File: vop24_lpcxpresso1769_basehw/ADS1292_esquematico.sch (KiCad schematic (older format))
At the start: 50 parts, among them J401 Conn_01x02, J402 Conn_01x02, J403 Conn_01x02, J404 Conn_01x04, J405 Conn_01x04, J406 Conn_01x04, U401 ADS1292, U402 LM334, U403 LM334, U404 LM334

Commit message: Finalizada asociación de todos los footprints. Ver librerías froux-kicad
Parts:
- C401, C402, C403, C404, C405, C406, C407, C408, C409, C410, C411, C412, C413, C414, C415, C416, C417, C418, C419, C420: footprint (none) -> Capacitor_SMD:C_0805_2012Metric_Pad1.15x1.40mm_HandSolder
- J401, J402, J403: footprint (none) -> Connector_PinHeader_1.27mm:PinHeader_1x02_P1.27mm_Vertical
- J404, J405, J406: footprint (none) -> Connector_PinHeader_1.27mm:PinHeader_1x04_P1.27mm_Vertical
- R401, R402, R403, R404, R405, R406, R407, R408, R409, R410, R411, R412, R413, R414, R415, R416, R417, R418, R419, R420: footprint (none) -> Resistor_SMD:R_0805_2012Metric_Pad1.15x1.40mm_HandSolder

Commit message: PCB: componentes agrupados por zona
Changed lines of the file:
@@
 SENS1N
 Text Label 10400 1650 0    60   ~ 0
-SENS1N
+SENS1P
 Wire Wire Line
 	6200 3250 6700 3250
@@
 SENS2N
 Text Label 10450 3650 0    60   ~ 0
-SENS2N
+SENS2P
 Wire Notes Line
 	7750 2500 7750 4400
@@
 SENS3N
 Text Label 10450 5650 0    60   ~ 0
-SENS3N
+SENS3P
 Wire Notes Line
 	7750 4450 7750 6350

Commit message: PCB: posicionamiento preruteo. ESQ: cambio de footprint de conectores
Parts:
- J404, J405: footprint Connector_PinHeader_1.27mm:PinHeader_1x04_P1.27mm_Vertical -> Connector_PinSocket_2.54mm:PinSocket_1x04_P2.54mm_Vertical
- J406: footprint Connector_PinHeader_1.27mm:PinHeader_1x04_P1.27mm_Vertical -> CConnector_PinSocket_2.54mm:PinSocket_1x04_P2.54mm_Vertical
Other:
- note added: "Desacople de la alimentacion\ndel ADS1292. Poner los caps\ncerca de los pines de alimentacion\n."
- note removed: "Desacople de la alimentacion\ndel ADS1292. Poner los caps\ncerca de los pines de alimentacion\n"
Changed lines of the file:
@@
 DVCC
 Text Notes 2450 7050 0    60   ~ 0
-Desacople de la alimentacion\ndel ADS1292. Poner los caps\ncerca de los pines de alimentacion\n
+Desacople de la alimentacion\ndel ADS1292. Poner los caps\ncerca de los pines de alimentacion\n.
 Wire Wire Line
 	9150 900  9150 1550
@@
 F 0 "J404" V 8800 1700 50  0000 C CNN
 F 1 "Conn_01x04" V 8700 1600 50  0000 C CNN
-F 2 "Connector_PinHeader_1.27mm:PinHeader_1x04_P1.27mm_Vertical" H 8600 1650 50  0001 C CNN
+F 2 "Connector_PinSocket_2.54mm:PinSocket_1x04_P2.54mm_Vertical" H 8600 1650 50  0001 C CNN
 F 3 "~" H 8600 1650 50  0001 C CNN
 	1    8600 1650
@@
 F 0 "J405" V 8800 3750 50  0000 C CNN
 F 1 "Conn_01x04" V 8700 3600 50  0000 C CNN
-F 2 "Connector_PinHeader_1.27mm:PinHeader_1x04_P1.27mm_Vertical" H 8600 3650 50  0001 C CNN
+F 2 "Connector_PinSocket_2.54mm:PinSocket_1x04_P2.54mm_Vertical" H 8600 3650 50  0001 C CNN
 F 3 "~" H 8600 3650 50  0001 C CNN
 	1    8600 3650
@@
 F 0 "J406" V 8750 5500 50  0000 C CNN
 F 1 "Conn_01x04" V 8850 5600 50  0000 C CNN
-F 2 "Connector_PinHeader_1.27mm:PinHeader_1x04_P1.27mm_Vertical" H 8650 5650 50  0001 C CNN
+F 2 "CConnector_PinSocket_2.54mm:PinSocket_1x04_P2.54mm_Vertical" H 8650 5650 50  0001 C CNN
 F 3 "~" H 8650 5650 50  0001 C CNN
 	1    8650 5650

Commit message: PCB: ruteo e ubicacion de USB.    ESQ: cambios de etiquetas de gnd en usb
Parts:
- J406: footprint CConnector_PinSocket_2.54mm:PinSocket_1x04_P2.54mm_Vertical -> Connector_PinSocket_2.54mm:PinSocket_1x04_P2.54mm_Vertical
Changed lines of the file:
@@
 F 0 "J406" V 8750 5500 50  0000 C CNN
 F 1 "Conn_01x04" V 8850 5600 50  0000 C CNN
-F 2 "CConnector_PinSocket_2.54mm:PinSocket_1x04_P2.54mm_Vertical" H 8650 5650 50  0001 C CNN
+F 2 "Connector_PinSocket_2.54mm:PinSocket_1x04_P2.54mm_Vertical" H 8650 5650 50  0001 C CNN
 F 3 "~" H 8650 5650 50  0001 C CNN
 	1    8650 5650

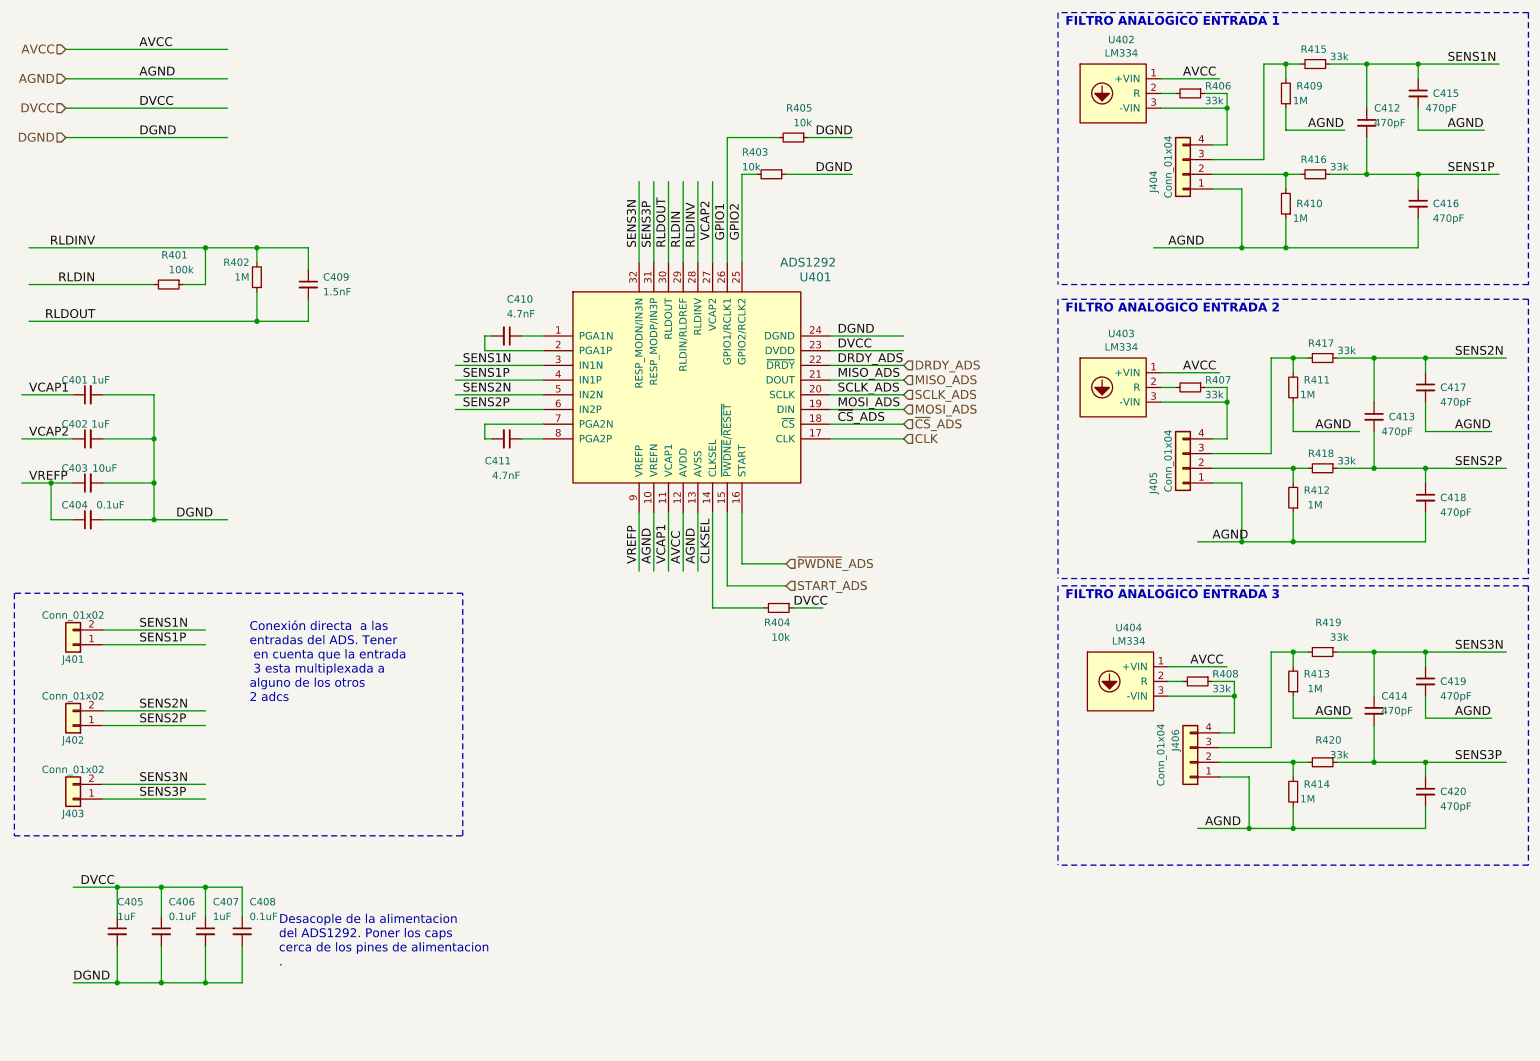
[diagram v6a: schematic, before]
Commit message: ESQ: modificaciones de etiquetas. Falta cambiar todas las conexiones de vcc
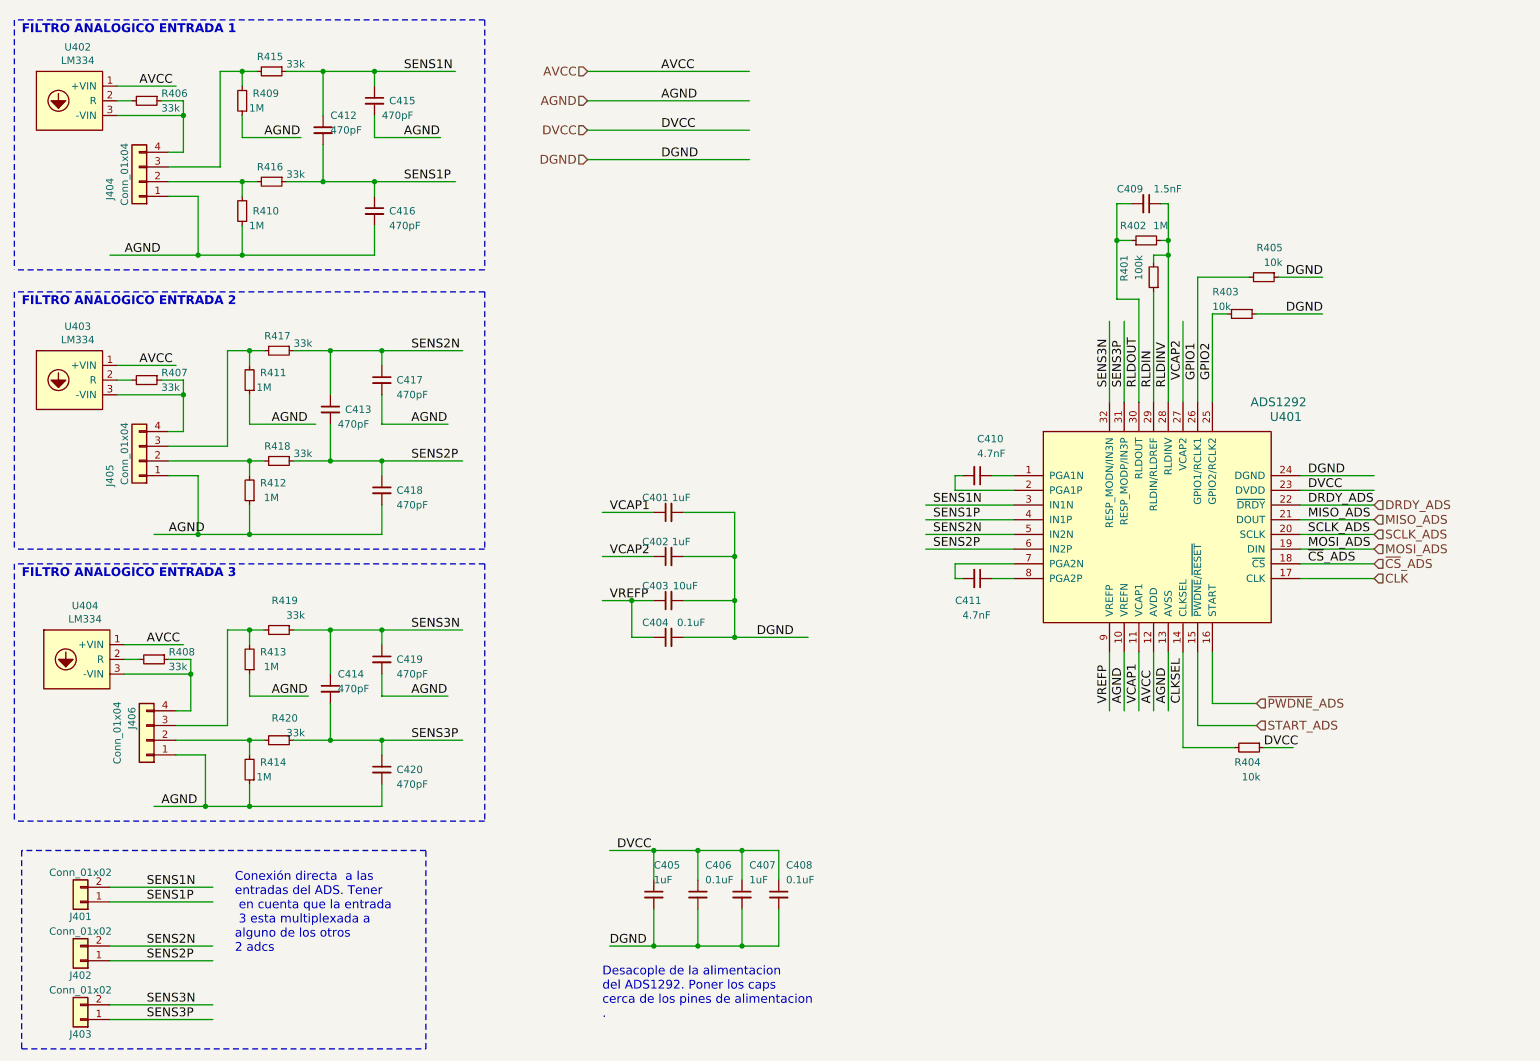
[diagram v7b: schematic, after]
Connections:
- wire segments 204 -> 203
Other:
- moved on the sheet: C401, C402, C403, C404, C405, C406, C407, C408, C409, C410, C411, C412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
